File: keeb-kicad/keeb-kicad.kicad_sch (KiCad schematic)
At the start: 0 parts

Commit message: Designed schematic replicating matrix and connecting rotary encoder
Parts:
- added A1: RaspberryPi_Pico, Module:RaspberryPi_Pico_Common_Unspecified, symbol MCU_Module:RaspberryPi_Pico
- added D1, D10, D11, D12, D13, D14, D15, D16, D17, D18, D19, D2, D20, D21, D22, D23, D24, D25, D26, D27, D28, D29, D3, D30, D31, D32, D33, D34, D35, D36, D37, D38, D39, D4, D40, D41, D42, D43, D44, D45, D46, D47, D48, D49, D5, D50, D51, D52, D53, D54, D55, D56, D57, D58, D59, D6, D60, D61, D62, D63, D64, D65, D66, D67, D68, D69, D7, D70, D8, D9: 1N4148, Diode_THT:D_DO-35_SOD27_P7.62mm_Horizontal, symbol Diode:1N4148
- added S1, S2, S3, S4, S5: MX_stab, PCM_marbastlib-mx:STAB_MX_P_6.25u, symbol PCM_marbastlib-mx:MX_stab
- added SW1, SW10, SW11, SW12, SW13, SW14, SW15, SW16, SW17, SW18, SW19, SW2, SW20, SW21, SW22, SW23, SW24, SW25, SW26, SW27, SW28, SW29, SW3, SW30, SW31, SW32, SW33, SW34, SW35, SW36, SW37, SW38, SW39, SW4, SW40, SW41, SW42, SW43, SW44, SW45, SW46, SW47, SW48, SW49, SW5, SW50, SW51, SW52, SW53, SW54, SW55, SW56, SW57, SW58, SW59, SW6, SW60, SW61, SW62, SW63, SW64, SW65, SW66, SW67, SW68, SW69, SW7, SW70, SW8, SW9: SW_Push, symbol Switch:SW_Push
- added SW71: RotaryEncoder_Switch, symbol Device:RotaryEncoder_Switch
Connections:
- new net: D54.2 (A), SW54.2
- new net: D47.2 (A), SW47.2
- new net: D59.2 (A), SW59.2
- new net: D4.2 (A), SW4.2
- new net: D70.2 (A), SW70.2
- new net: D57.2 (A), SW57.2
- new net: D67.2 (A), SW67.2
- new net: D58.2 (A), SW58.2
- new net: D42.2 (A), SW42.2
- new net: D66.2 (A), SW66.2
- new net: D8.2 (A), SW8.2
- new net: D19.2 (A), SW19.2
- new net: D31.2 (A), SW31.2
- new net: D15.2 (A), SW15.2
- new net: D6.2 (A), SW6.2
- new net: D28.2 (A), SW28.2
- new net: D5.2 (A), SW5.2
- new net: D64.2 (A), SW64.2
- new net: D43.2 (A), SW43.2
- new net: D20.2 (A), SW20.2
- new net: D16.2 (A), SW16.2
- new net: D33.2 (A), SW33.2
- new net: D32.2 (A), SW32.2
- new net: D65.2 (A), SW65.2
- new net: D55.2 (A), SW55.2
- new net: D23.2 (A), SW23.2
- new net: D38.2 (A), SW38.2
- new net: D13.2 (A), SW13.2
- new net: D44.2 (A), SW44.2
- new net: D36.2 (A), SW36.2
- new net: D63.2 (A), SW63.2
- new net: D14.2 (A), SW14.2
- new net: D41.2 (A), SW41.2
- new net: D56.2 (A), SW56.2
- new net: D25.2 (A), SW25.2
- new net: D39.2 (A), SW39.2
- new net: D61.2 (A), SW61.2
- new net: D52.2 (A), SW52.2
- new net: D50.2 (A), SW50.2
- new net: D51.2 (A), SW51.2
- new net: D21.2 (A), SW21.2
- new net: D3.2 (A), SW3.2
- new net: D40.2 (A), SW40.2
- new net: D1.2 (A), SW1.2
- new net: D27.2 (A), SW27.2
- new net: D18.2 (A), SW18.2
- new net: D49.2 (A), SW49.2
- new net: D53.2 (A), SW53.2
- new net: D11.2 (A), SW11.2
- new net: D48.2 (A), SW48.2
- new net: D45.2 (A), SW45.2
- new net: D37.2 (A), SW37.2
- new net: D68.2 (A), SW68.2
- new net: D26.2 (A), SW26.2
- new net: D60.2 (A), SW60.2
- new net: D22.2 (A), SW22.2
- new net: D10.2 (A), SW10.2
- new net: D34.2 (A), SW34.2
- new net: D9.2 (A), SW9.2
- new net: D2.2 (A), SW2.2
- new net: D7.2 (A), SW7.2
- new net: D69.2 (A), SW69.2
- new net: D17.2 (A), SW17.2
- new net: D29.2 (A), SW29.2
- new net: D24.2 (A), SW24.2
- new net: D12.2 (A), SW12.2
- new net: D30.2 (A), SW30.2
- new net: D35.2 (A), SW35.2
- new net: D46.2 (A), SW46.2
- new net: D62.2 (A), SW62.2
- new net COL0: A1.7 (GPIO5), SW1.1, SW16.1, SW32.1, SW46.1, SW60.1
- new net COL1: A1.9 (GPIO6), SW17.1, SW2.1, SW33.1, SW47.1, SW61.1
- new net COL10: A1.20 (GPIO15), SW11.1, SW26.1, SW42.1, SW55.1, SW65.1
- new net COL11: A1.21 (GPIO16), SW12.1, SW27.1, SW43.1, SW66.1
- new net COL12: A1.22 (GPIO17), SW13.1, SW28.1, SW56.1, SW67.1
- new net COL13: A1.24 (GPIO18), SW14.1, SW29.1, SW44.1, SW68.1
- new net COL14: A1.25 (GPIO19), SW30.1, SW57.1, SW69.1
- new net COL15: A1.26 (GPIO20), SW15.1, SW31.1, SW45.1, SW58.1, SW70.1
- new net COL2: A1.10 (GPIO7), SW18.1, SW3.1, SW34.1, SW59.1, SW62.1
- new net COL3: A1.11 (GPIO8), SW19.1, SW35.1, SW4.1, SW48.1, SW63.1
- new net COL4: A1.12 (GPIO9), SW20.1, SW36.1, SW49.1, SW5.1
- new net COL5: A1.14 (GPIO10), SW21.1, SW37.1, SW50.1, SW6.1
- new net COL6: A1.15 (GPIO11), SW22.1, SW38.1, SW51.1, SW64.1, SW7.1
- new net COL7: A1.16 (GPIO12), SW23.1, SW39.1, SW52.1, SW8.1
- new net COL8: A1.17 (GPIO13), SW24.1, SW40.1, SW53.1, SW9.1
- new net COL9: A1.19 (GPIO14), SW10.1, SW25.1, SW41.1, SW54.1
- new net ENC_A: A1.27 (GPIO21), SW71.A
- new net ENC_B: A1.29 (GPIO22), SW71.B
- new net GND: A1.13 (GND), A1.18 (GND), A1.23 (GND), A1.28 (GND), A1.3 (GND), A1.38 (GND), A1.8 (GND), SW71.C, SW71.S2
- new net ROW0: A1.1 (GPIO0), D1.1 (K), D10.1 (K), D11.1 (K), D12.1 (K), D13.1 (K), D14.1 (K), D15.1 (K), D2.1 (K), D3.1 (K), D4.1 (K), D5.1 (K), D6.1 (K), D7.1 (K), D8.1 (K), D9.1 (K)
- new net ROW1: A1.2 (GPIO1), D16.1 (K), D17.1 (K), D18.1 (K), D19.1 (K), D20.1 (K), D21.1 (K), D22.1 (K), D23.1 (K), D24.1 (K), D25.1 (K), D26.1 (K), D27.1 (K), D28.1 (K), D29.1 (K), D30.1 (K), D31.1 (K)
- new net ROW2: A1.4 (GPIO2), D32.1 (K), D33.1 (K), D34.1 (K), D35.1 (K), D36.1 (K), D37.1 (K), D38.1 (K), D39.1 (K), D40.1 (K), D41.1 (K), D42.1 (K), D43.1 (K), D44.1 (K), D45.1 (K)
- new net ROW3: A1.5 (GPIO3), D46.1 (K), D47.1 (K), D48.1 (K), D49.1 (K), D50.1 (K), D51.1 (K), D52.1 (K), D53.1 (K), D54.1 (K), D55.1 (K), D56.1 (K), D57.1 (K), D58.1 (K)
- new net ROW4: A1.6 (GPIO4), D60.1 (K), D61.1 (K), D62.1 (K), D63.1 (K), D64.1 (K), D65.1 (K), D66.1 (K), D67.1 (K), D68.1 (K), D69.1 (K), D70.1 (K)
- new net SW1: A1.31 (GPIO26_ADC0), SW71.S1

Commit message: Changed sizing of specific keys in keyboard, placed top two rows swtiches on pcb board
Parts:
- added SW72: RotaryEncoder_Switch, symbol Device:RotaryEncoder_Switch
- A1: footprint Module:RaspberryPi_Pico_Common_Unspecified -> Module:RaspberryPi_Pico_Common_THT
- S1: footprint PCM_marbastlib-mx:STAB_MX_P_6.25u -> PCM_marbastlib-mx:STAB_MX_P_2.25u
- S2: footprint PCM_marbastlib-mx:STAB_MX_P_6.25u -> PCM_marbastlib-mx:STAB_MX_P_2.75u
- S4: footprint PCM_marbastlib-mx:STAB_MX_P_6.25u -> PCM_marbastlib-mx:STAB_MX_P_2u
- SW1, SW10, SW11, SW12, SW13, SW14, SW15, SW16, SW17, SW18, SW19, SW2, SW20, SW21, SW22, SW23, SW24, SW25, SW26, SW27, SW28, SW29, SW3, SW30, SW31, SW32, SW33, SW34, SW35, SW36, SW37, SW38, SW39, SW4, SW40, SW41, SW42, SW43, SW44, SW45, SW46, SW47, SW48, SW49, SW5, SW50, SW51, SW52, SW53, SW54, SW55, SW56, SW57, SW58, SW59, SW6, SW60, SW61, SW62, SW63, SW64, SW65, SW66, SW67, SW68, SW69, SW7, SW70, SW8, SW9: footprint (none) -> PCM_marbastlib-mx:SW_MX_1u
- SW71: footprint (none) -> Rotary_Encoder:RotaryEncoder_Alps_EC11E-Switch_Vertical_H20mm
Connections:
- net ENC_A: now also SW72.A
- net ENC_B: now also SW72.B
- net GND: now also SW72.C, SW72.S2
- net SW1 renamed SWITCH1
- net SWITCH1: now also SW72.S1

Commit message: Finished PCB assembly of keyboard switches
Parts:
- removed SW71: RotaryEncoder_Switch, Rotary_Encoder:RotaryEncoder_Alps_EC11E-Switch_Vertical_H20mm, symbol Device:RotaryEncoder_Switch
- S1: footprint PCM_marbastlib-mx:STAB_MX_P_2.25u -> PCM_marbastlib-mx:STAB_MX_P_2.75u
- S3: footprint PCM_marbastlib-mx:STAB_MX_P_6.25u -> PCM_marbastlib-mx:STAB_MX_P_2u
- S4: footprint PCM_marbastlib-mx:STAB_MX_P_2u -> PCM_marbastlib-mx:STAB_MX_P_3u
- SW71: renamed from SW72; footprint (none) -> Rotary_Encoder:RotaryEncoder_Alps_EC11E-Switch_Vertical_H20mm
- renumbered SW59 to SW48, SW48 to SW49, SW49 to SW50, SW50 to SW51, SW51 to SW52, SW52 to SW53, SW53 to SW54, SW54 to SW55, SW55 to SW56, SW56 to SW57, SW57 to SW58, SW58 to SW59
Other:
- moved on the sheet: SW71

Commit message: Placed rest of the components onto PCB
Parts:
- renumbered D59 to D48, D48 to D49, D49 to D50, D50 to D51, D51 to D52, D52 to D53, D53 to D54, D54 to D55, D55 to D56, D56 to D57, D57 to D58, D58 to D59
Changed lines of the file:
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@@
 		(in_pos_files yes)
 		(dnp no)
-		(property "Reference" "D59"
+		(property "Reference" "D48"
 			(at 62.23 96.865 90)
 			(show_name no)
@@
 			(project "keeb-kicad"
 				(path "/e712c4fd-eb72-4b90-816e-2a87f9f0352e"
-					(reference "D59")
+					(reference "D48")
 					(unit 1)
 				)
@@
 		(in_pos_files yes)
 		(dnp no)
-		(property "Reference" "D57"
+		(property "Reference" "D58"
 			(at 229.87 96.5199 90)
 			(show_name no)
@@
 			(project "keeb-kicad"
 				(path "/e712c4fd-eb72-4b90-816e-2a87f9f0352e"
-					(reference "D57")
+					(reference "D58")
 					(unit 1)
 				)
@@
 		(in_pos_files yes)
 		(dnp no)
-		(property "Reference" "D55"
+		(property "Reference" "D56"
 			(at 173.99 96.5199 90)
 			(show_name no)
@@
 			(project "keeb-kicad"
 				(path "/e712c4fd-eb72-4b90-816e-2a87f9f0352e"
-					(reference "D55")
+					(reference "D56")
 					(unit 1)
 				)
@@
 		(in_pos_files yes)
 		(dnp no)
-		(property "Reference" "D56"
+		(property "Reference" "D57"
 			(at 201.93 96.5199 90)
 			(show_name no)
@@
 			(project "keeb-kicad"
 				(path "/e712c4fd-eb72-4b90-816e-2a87f9f0352e"
-					(reference "D56")
+					(reference "D57")
 					(unit 1)
 				)
@@
 		(in_pos_files yes)
 		(dnp no)
-		(property "Reference" "D52"
+		(property "Reference" "D53"
 			(at 132.08 96.5199 90)
 			(show_name no)
@@
 			(project "keeb-kicad"
 				(path "/e712c4fd-eb72-4b90-816e-2a87f9f0352e"
-					(reference "D52")
+					(reference "D53")
 					(unit 1)
 				)
@@
 		(in_pos_files yes)
 		(dnp no)
-		(property "Reference" "D58"
+		(property "Reference" "D59"
 			(at 243.84 96.5199 90)
 			(show_name no)
@@
 			(project "keeb-kicad"
 				(path "/e712c4fd-eb72-4b90-816e-2a87f9f0352e"
-					(reference "D58")
+					(reference "D59")
 					(unit 1)
 				)
@@
 		(in_pos_files yes)
 		(dnp no)
-		(property "Reference" "D51"
+		(property "Reference" "D52"
 			(at 118.11 96.5199 90)
 			(show_name no)
@@
 			(project "keeb-kicad"
 				(path "/e712c4fd-eb72-4b90-816e-2a87f9f0352e"
-					(reference "D51")
+					(reference "D52")
 					(unit 1)
 				)
@@
 		(in_pos_files yes)
 		(dnp no)
-		(property "Reference" "D49"
+		(property "Reference" "D50"
 			(at 90.17 96.5199 90)
 			(show_name no)
@@
 			(project "keeb-kicad"
 				(path "/e712c4fd-eb72-4b90-816e-2a87f9f0352e"
-					(reference "D49")
+					(reference "D50")
 					(unit 1)
 				)
@@
 		(in_pos_files yes)
 		(dnp no)
-		(property "Reference" "D53"
+		(property "Reference" "D54"
 			(at 146.05 96.5199 90)
 			(show_name no)
@@
 			(project "keeb-kicad"
 				(path "/e712c4fd-eb72-4b90-816e-2a87f9f0352e"
-					(reference "D53")
+					(reference "D54")
 					(unit 1)
 				)
@@
 		(in_pos_files yes)
 		(dnp no)
-		(property "Reference" "D54"
+		(property "Reference" "D55"
 			(at 160.02 96.5199 90)
 			(show_name no)
@@
 			(project "keeb-kicad"
 				(path "/e712c4fd-eb72-4b90-816e-2a87f9f0352e"
-					(reference "D54")
+					(reference "D55")
 					(unit 1)
 				)
@@
 		(in_pos_files yes)
 		(dnp no)
-		(property "Reference" "D50"
+		(property "Reference" "D51"
 			(at 104.14 96.5199 90)
 			(show_name no)
@@
 			(project "keeb-kicad"
 				(path "/e712c4fd-eb72-4b90-816e-2a87f9f0352e"
-					(reference "D50")
+					(reference "D51")
 					(unit 1)
 				)
@@
 		(in_pos_files yes)
 		(dnp no)
-		(property "Reference" "D48"
+		(property "Reference" "D49"
 			(at 76.2 96.5199 90)
 			(show_name no)
@@
 			(project "keeb-kicad"
 				(path "/e712c4fd-eb72-4b90-816e-2a87f9f0352e"
-					(reference "D48")
+					(reference "D49")
 					(unit 1)
 				)

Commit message: Added route tracing to front side of PCB
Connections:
- net COL0: now also A1.1 (GPIO0); no longer A1.7 (GPIO5)
- net COL1: now also A1.2 (GPIO1); no longer A1.9 (GPIO6)
- net COL10: now also A1.14 (GPIO10); no longer A1.20 (GPIO15)
- net COL11: now also A1.15 (GPIO11); no longer A1.21 (GPIO16)
- net COL12: now also A1.16 (GPIO12); no longer A1.22 (GPIO17)
- net COL13: now also A1.17 (GPIO13); no longer A1.24 (GPIO18)
- net COL14: now also A1.19 (GPIO14); no longer A1.25 (GPIO19)
- net COL15: now also A1.20 (GPIO15); no longer A1.26 (GPIO20)
- net COL2: now also A1.4 (GPIO2); no longer A1.10 (GPIO7)
- net COL3: now also A1.5 (GPIO3); no longer A1.11 (GPIO8)
- net COL4: now also A1.6 (GPIO4); no longer A1.12 (GPIO9)
- net COL5: now also A1.7 (GPIO5); no longer A1.14 (GPIO10)
- net COL6: now also A1.9 (GPIO6); no longer A1.15 (GPIO11)
- net COL7: now also A1.10 (GPIO7); no longer A1.16 (GPIO12)
- net COL8: now also A1.11 (GPIO8); no longer A1.17 (GPIO13)
- net COL9: now also A1.12 (GPIO9); no longer A1.19 (GPIO14)
- net ENC_A: now also A1.24 (GPIO18); no longer A1.27 (GPIO21)
- net ENC_B: now also A1.22 (GPIO17); no longer A1.29 (GPIO22)
- net ROW0: now also A1.25 (GPIO19); no longer A1.1 (GPIO0)
- net ROW1: now also A1.26 (GPIO20); no longer A1.2 (GPIO1)
- net ROW2: now also A1.27 (GPIO21); no longer A1.4 (GPIO2)
- net ROW3: now also A1.29 (GPIO22); no longer A1.5 (GPIO3)
- net ROW4: now also A1.31 (GPIO26_ADC0); no longer A1.6 (GPIO4)
- net SWITCH1: now also A1.21 (GPIO16); no longer A1.31 (GPIO26_ADC0)
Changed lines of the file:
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@@
 		)
 	)
-	(label "COL12"
+	(label "ENC_B"
 		(at 165.1 151.13 180)
 		(effects
@@
 		)
 	)
-	(label "SWITCH1"
+	(label "ROW4"
 		(at 163.83 173.99 180)
 		(effects
@@
 		)
 	)
-	(label "COL9"
+	(label "COL14"
 		(at 104.14 181.61 0)
 		(effects
@@
 		)
 	)
-	(label "COL15"
+	(label "ROW1"
 		(at 165.1 158.75 180)
 		(effects
@@
 		)
 	)
-	(label "ROW0"
+	(label "COL0"
 		(at 104.14 146.05 0)
 		(effects
@@
 		)
 	)
-	(label "COL4"
+	(label "COL9"
 		(at 104.14 168.91 0)
 		(effects
@@
 		)
 	)
-	(label "ENC_B"
+	(label "ROW3"
 		(at 165.1 163.83 180)
 		(effects
@@
 		)
 	)
-	(label "ROW2"
+	(label "COL2"
 		(at 104.14 151.13 0)
 		(effects
@@
 		)
 	)
-	(label "COL1"
+	(label "COL6"
 		(at 104.14 161.29 0)
 		(effects
@@
 		)
 	)
-	(label "COL7"
+	(label "COL12"
 		(at 104.14 176.53 0)
 		(effects
@@
 		)
 	)
-	(label "COL3"
+	(label "COL8"
 		(at 104.14 166.37 0)
 		(effects
@@
 		)
 	)
-	(label "ROW4"
+	(label "COL4"
 		(at 104.14 156.21 0)
 		(effects
@@
 		)
 	)
-	(label "COL10"
+	(label "COL15"
 		(at 104.14 184.15 0)
 		(effects
@@
 		)
 	)
-	(label "COL6"
+	(label "COL11"
 		(at 104.14 173.99 0)
 		(effects
@@
 		)
 	)
-	(label "COL14"
+	(label "ROW0"
 		(at 165.1 156.21 180)
 		(effects
@@
 		)
 	)
-	(label "COL2"
+	(label "COL7"
 		(at 104.14 163.83 0)
 		(effects
@@
 		)
 	)
-	(label "COL5"
+	(label "COL10"
 		(at 104.14 171.45 0)
 		(effects
@@
 		)
 	)
-	(label "ENC_A"
+	(label "ROW2"
 		(at 165.1 161.29 180)
 		(effects
@@
 		)
 	)
-	(label "COL0"
+	(label "COL5"
 		(at 104.14 158.75 0)
 		(effects
@@
 		)
 	)
-	(label "COL8"
+	(label "COL13"
 		(at 104.14 179.07 0)
 		(effects
@@
 		)
 	)
-	(label "ROW1"
+	(label "COL1"
 		(at 104.14 148.59 0)
 		(effects
@@
 		)
 	)
-	(label "COL11"
+	(label "SWITCH1"
 		(at 165.1 148.59 180)
 		(effects
@@
 		)
 	)
-	(label "COL13"
+	(label "ENC_A"
 		(at 165.1 153.67 180)
 		(effects
@@
 		)
 	)
-	(label "ROW3"
+	(label "COL3"
 		(at 104.14 153.67 0)
 		(effects

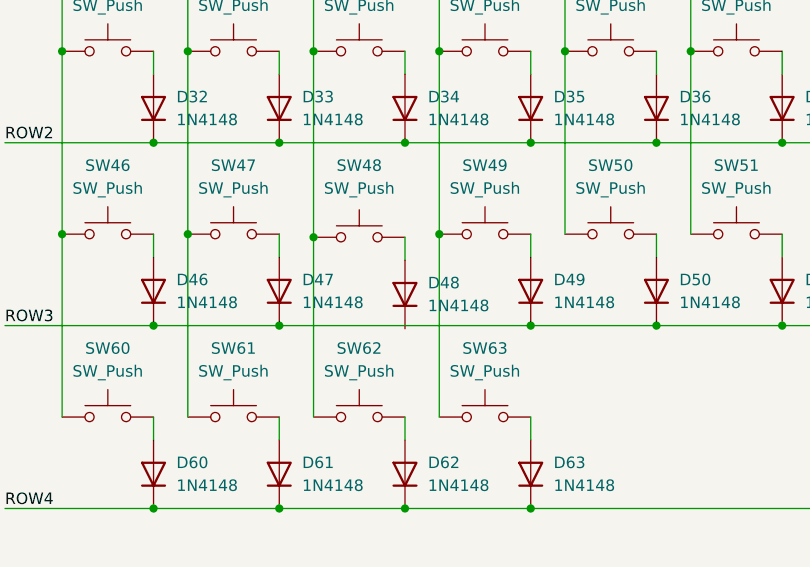
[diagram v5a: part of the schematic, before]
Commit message: Finished route tracing and added ground fill
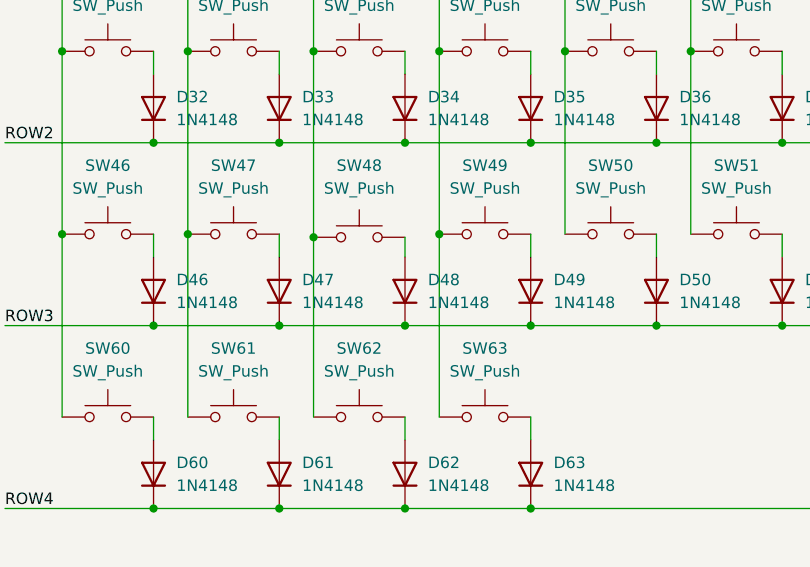
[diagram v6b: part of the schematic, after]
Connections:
- net ROW3: now also D48.1 (K)
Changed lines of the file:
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@@
 	)
 	(junction
+		(at 59.69 101.6)
+		(diameter 0)
+		(color 0 0 0 0)
+	)
+	(junction
 		(at 35.56 91.44)
 		(diameter 0)
@@
 	(wire
 		(pts
-			(xy 59.69 91.7851) (xy 59.69 94.3251)
+			(xy 59.69 91.7851) (xy 59.69 93.98)
 		)
 		(stroke
@@
 	(wire
 		(pts
-			(xy 45.72 101.6) (xy 73.66 101.6)
+			(xy 45.72 101.6) (xy 59.69 101.6)
 		)
 		(stroke
@@
 	(wire
 		(pts
+			(xy 59.69 101.6) (xy 73.66 101.6)
+		)
+		(stroke
+			(width 0)
+			(type default)
+		)
+	)
+	(wire
+		(pts
 			(xy 161.29 91.44) (xy 161.29 111.76)
 		)
@@
 	(symbol
 		(lib_id "Diode:1N4148")
-		(at 59.69 98.1351 90)
+		(at 59.69 97.79 90)
 		(unit 1)
 		(body_style 1)
@@
 		(dnp no)
 		(property "Reference" "D48"
-			(at 62.23 96.865 90)
+			(at 62.23 96.5199 90)
 			(show_name no)
 			(do_not_autoplace no)
@@
 		)
 		(property "Value" "1N4148"
-			(at 62.23 99.405 90)
+			(at 62.23 99.0599 90)
 			(show_name no)
 			(do_not_autoplace no)
@@
 		)
 		(property "Footprint" "Diode_THT:D_DO-35_SOD27_P7.62mm_Horizontal"
-			(at 59.69 98.1351 0)
+			(at 59.69 97.79 0)
 			(hide yes)
 			(show_name no)
@@
 		)
 		(property "Datasheet" "https://assets.nexperia.com/documents/data-sheet/1N4148_1N4448.pdf"
-			(at 59.69 98.1351 0)
+			(at 59.69 97.79 0)
 			(hide yes)
 			(show_name no)
@@
 		)
 		(property "Description" "100V 0.15A standard switching diode, DO-35"
-			(at 59.69 98.1351 0)
+			(at 59.69 97.79 0)
 			(hide yes)
 			(show_name no)
@@
 		)
 		(property "Sim.Device" "D"
-			(at 59.69 98.1351 0)
+			(at 59.69 97.79 0)
 			(hide yes)
 			(show_name no)
@@
 		)
 		(property "Sim.Pins" "1=K 2=A"
-			(at 59.69 98.1351 0)
+			(at 59.69 97.79 0)
 			(hide yes)
 			(show_name no)
